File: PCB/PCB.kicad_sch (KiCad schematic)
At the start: 27 parts, among them J1 USB_C_Receptacle_USB2.0_16P, SW1 SW_Push, U1 RP2040, U2 USBLC6-2SC6, U3 NCP1117ST33T3G, Y1 Crystal_GND24

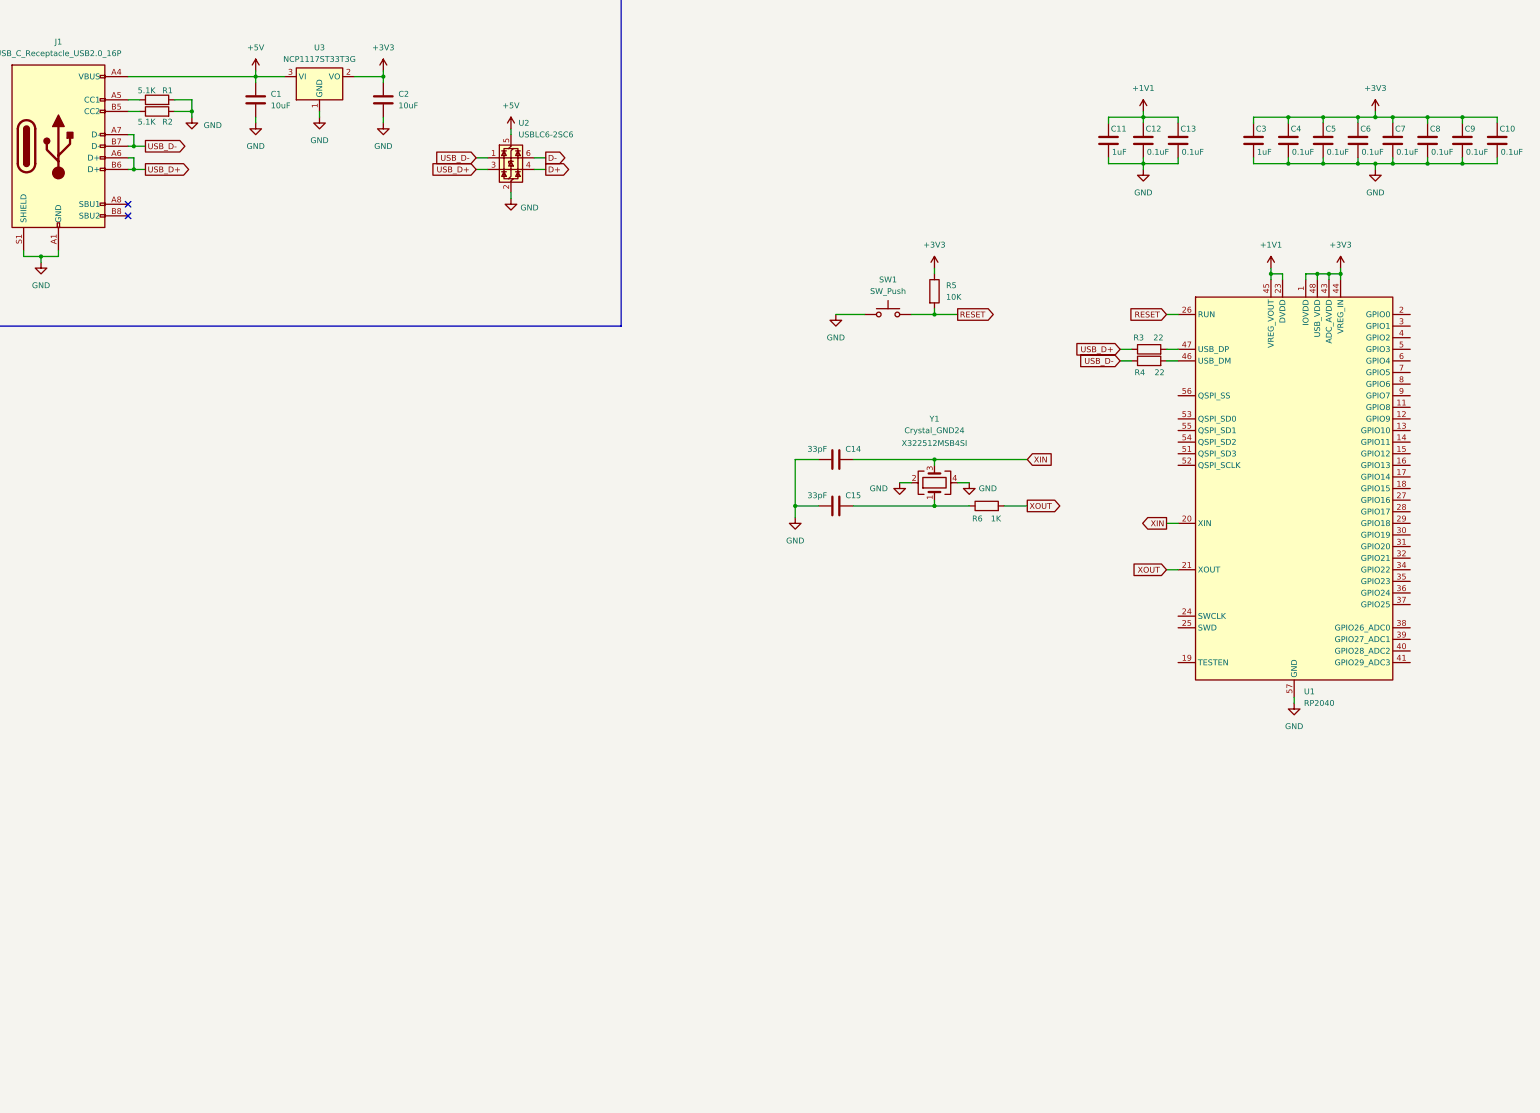
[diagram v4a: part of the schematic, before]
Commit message: added the flash
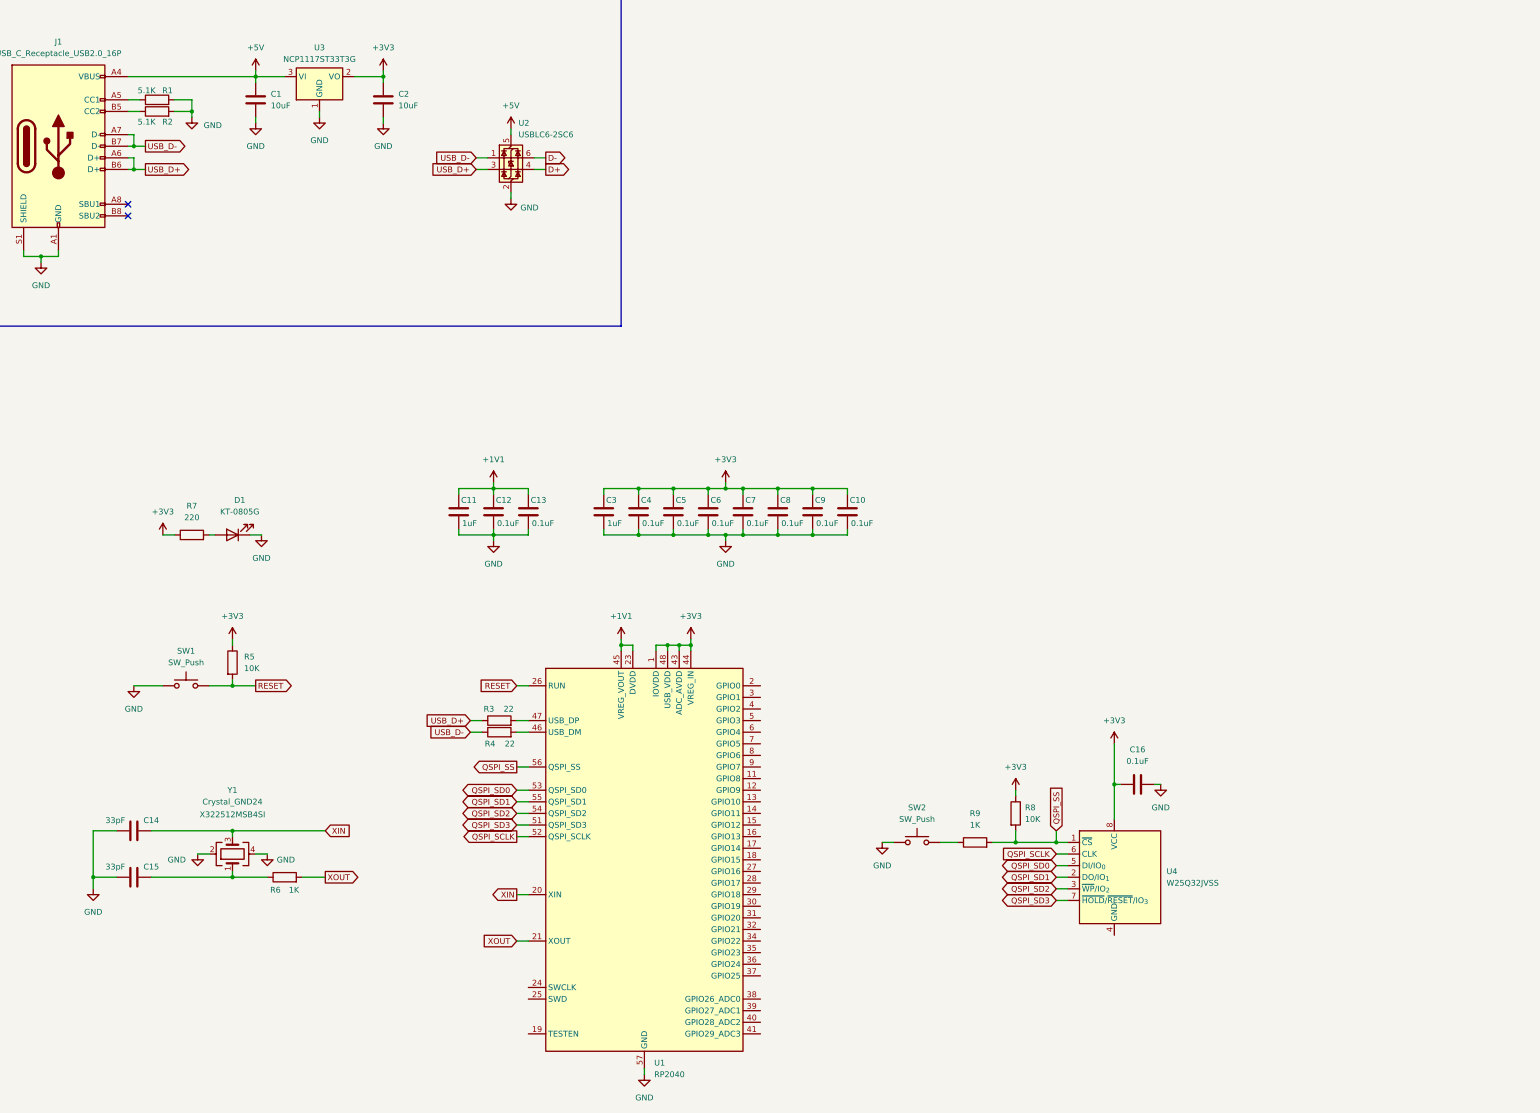
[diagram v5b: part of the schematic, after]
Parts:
- added C16: 0.1uF, symbol Device:C
- added D1: KT-0805G, symbol Device:LED
- added R7: 220, symbol Device:R
- added R8: 10K, symbol Device:R
- added R9: 1K, symbol Device:R
- added SW2: SW_Push, symbol Switch:SW_Push
- added U4: W25Q32JVSS, Package_SO:SOIC-8_5.3x5.3mm_P1.27mm, symbol Memory_Flash:W25Q32JVSS
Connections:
- net +3V3: now also C16.1, R7.1, R8.1, U4.8 (VCC)
- net GND: now also C16.2, D1.1 (K), SW2.1
- net QSPI_SD3: now reaches U1.51 (QSPI_SD3)
- net QSPI_SD3: now also U4.7 (~{HOLD}/~{RESET}/IO_{3})
- net QSPI_SCLK: now reaches U1.52 (QSPI_SCLK)
- net QSPI_SCLK: now also U4.6 (CLK)
- net QSPI_SD0: now reaches U1.53 (QSPI_SD0)
- net QSPI_SD0: now also U4.5 (DI/IO_{0})
- net QSPI_SD2: now reaches U1.54 (QSPI_SD2)
- net QSPI_SD2: now also U4.3 (~{WP}/IO_{2})
- net QSPI_SD1: now reaches U1.55 (QSPI_SD1)
- net QSPI_SD1: now also U4.2 (DO/IO_{1})
- net QSPI_SS: now reaches U1.56 (QSPI_SS)
- net QSPI_SS: now also R8.2, R9.2, U4.1 (~{CS})
- new net: R9.1, SW2.2
- new net: D1.2 (A), R7.2
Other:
- moved on the sheet: C10, C11, C12, C13, C14, C15, C3, C4, C5, C6, C7, C8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

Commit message: added the FPC connector in
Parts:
- added FPC1: AFC07-S24FCA-00, easyeda2kicad:FPC-SMD_AFC07-S24FCA-00, symbol easyeda2kicad:AFC07-S24FCA-00
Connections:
- net GND: now also U4.4 (GND)
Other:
- note added: "https://www.waveshare.com/w/upload/8/87/E-Paper-Driver-HAT-Schematic.pdf"
- moved on the sheet: C10, C11, C12, C13, C14, C15, C16, C3, C4, C5, C6, C7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

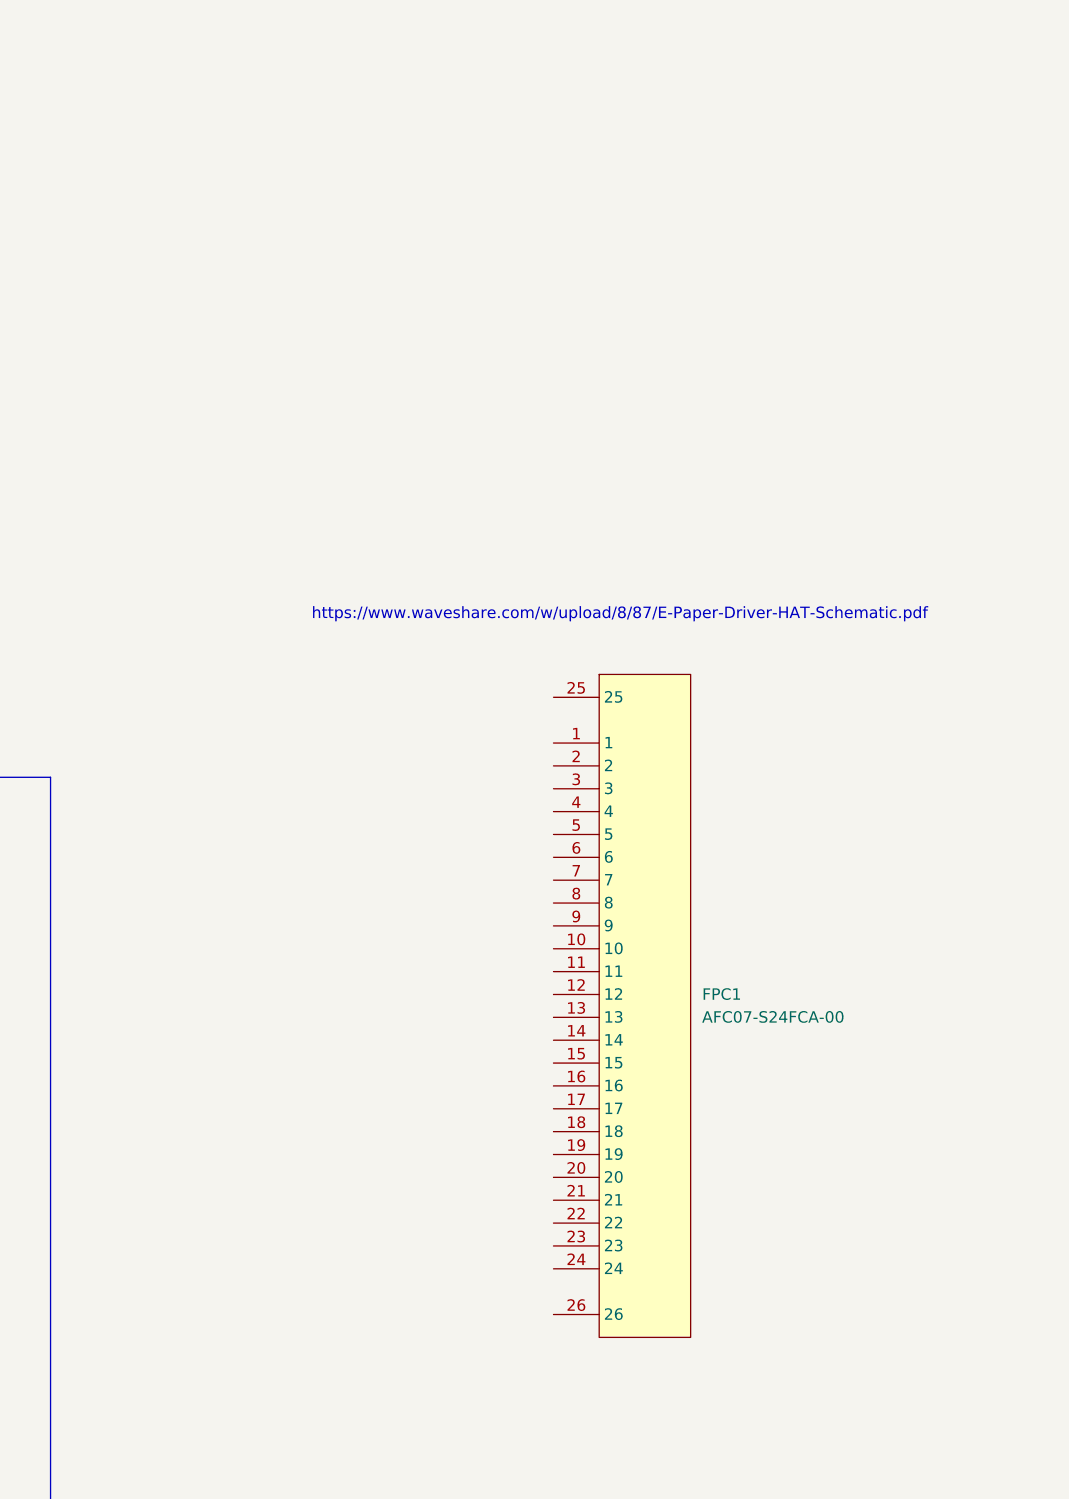
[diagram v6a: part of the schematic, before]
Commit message: changing the FPC symbol and starting to wire it
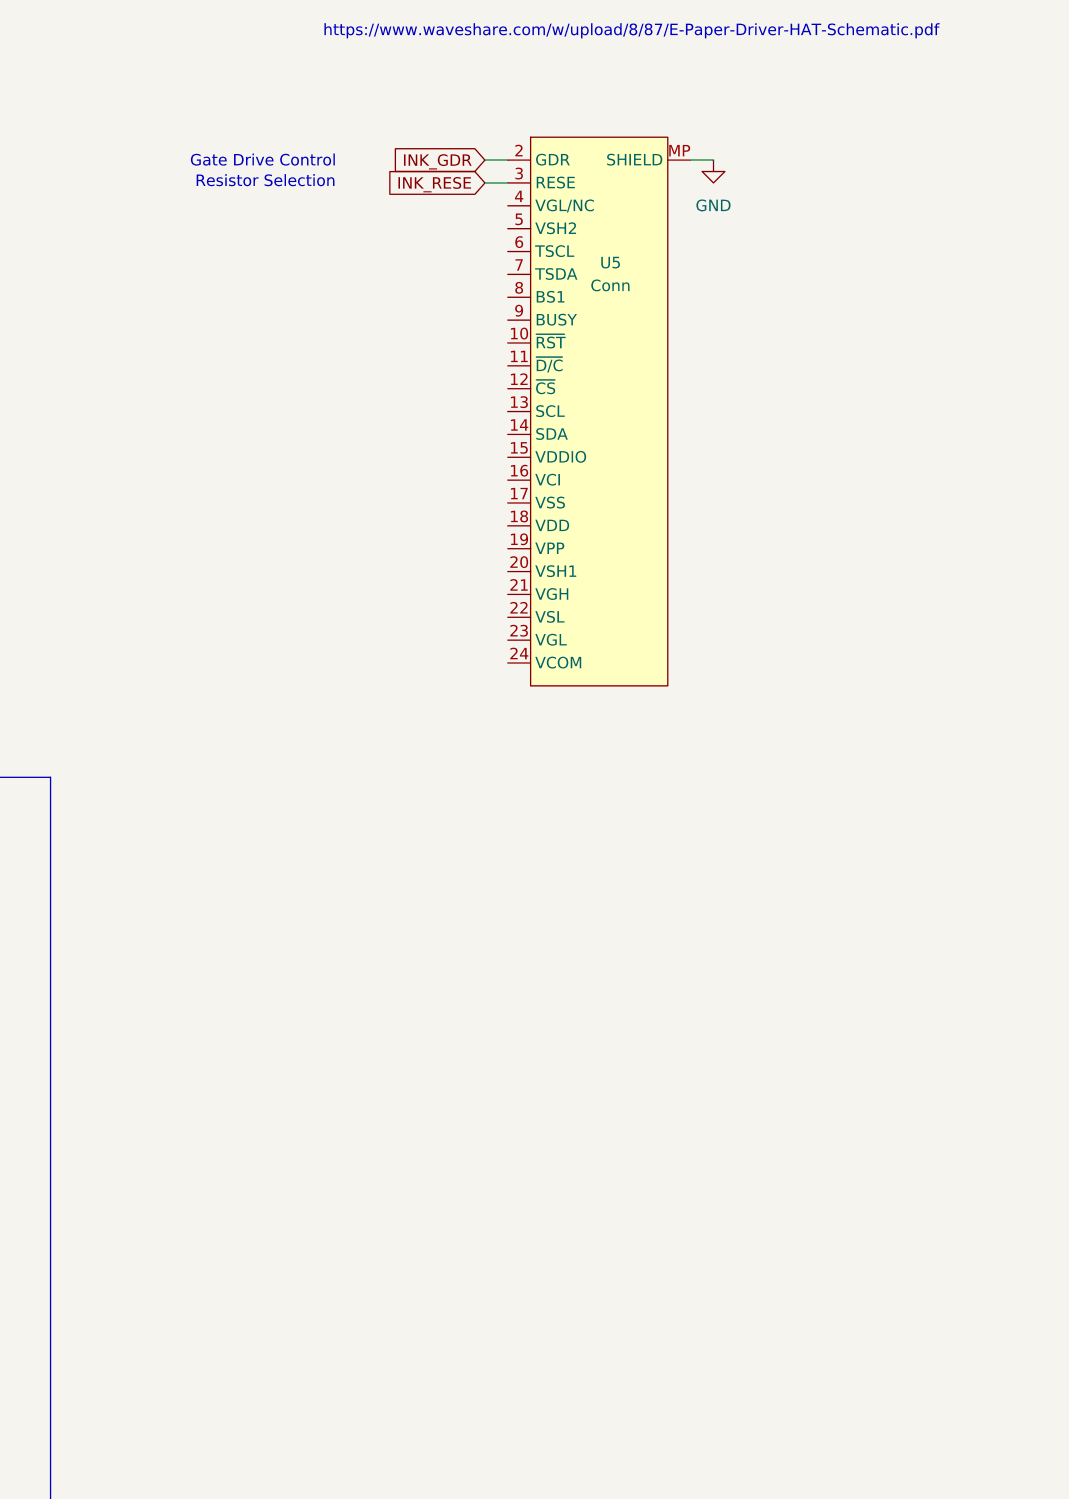
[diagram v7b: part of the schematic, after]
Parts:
- removed FPC1: AFC07-S24FCA-00, easyeda2kicad:FPC-SMD_AFC07-S24FCA-00, symbol easyeda2kicad:AFC07-S24FCA-00
- added U5: Conn, inkbadge:LCSC_1x24-1MP_P0.5mm_Horizontal, symbol inkbadge:EINK-2.9inch
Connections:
- net GND: now also U5.MP (SHIELD)
- new net INK_GDR: U5.2 (GDR)
- new net INK_RESE: U5.3 (RESE)
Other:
- note added: "Gate Drive Control"
- note added: "Resistor Selection"
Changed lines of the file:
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@@
 	(text "https://www.waveshare.com/w/upload/8/87/E-Paper-Driver-HAT-Schematic.pdf"
 		(exclude_from_sim no)
-		(at 356.616 77.216 0)
+		(at 357.886 12.446 0)
+		(effects
+			(font
+				(size 1.27 1.27)
+			)
+		)
+	)
+	(text "Resistor Selection"
+		(exclude_from_sim no)
+		(at 317.246 29.21 0)
+		(effects
+			(font
+				(size 1.27 1.27)
+			)
+		)
+	)
+	(text "Gate Drive Control"
+		(exclude_from_sim no)
+		(at 316.992 26.924 0)
 		(effects
 			(font
@@
 	(wire
 		(pts
+			(xy 341.63 26.67) (xy 344.17 26.67)
+		)
+		(stroke
+			(width 0)
+			(type default)
+		)
+	)
+	(wire
+		(pts
 			(xy 124.46 181.61) (xy 127 181.61)
 		)
@@
 	(wire
 		(pts
+			(xy 341.63 29.21) (xy 344.17 29.21)
+		)
+		(stroke
+			(width 0)
+			(type default)
+		)
+	)
+	(wire
+		(pts
 			(xy 57.15 138.43) (xy 58.42 138.43)
 		)
@@
 	(wire
 		(pts
+			(xy 367.03 26.67) (xy 364.49 26.67)
+		)
+		(stroke
+			(width 0)
+			(type default)
+		)
+	)
+	(wire
+		(pts
 			(xy 111.76 138.43) (xy 119.38 138.43)
 		)
@@
 		)
 	)
+	(global_label "INK_RESE"
+		(shape input)
+		(at 341.63 29.21 180)
+		(fields_autoplaced yes)
+		(effects
+			(font
+				(size 1.27 1.27)
+			)
+			(justify right)
+		)
+		(property "Intersheetrefs" "${INTERSHEET_REFS}"
+			(at 329.6944 29.21 0)
+			(effects
+				(font
+					(size 1.27 1.27)
+				)
+				(justify right)
+				(hide yes)
+			)
+		)
+	)
+	(global_label "INK_GDR"
+		(shape input)
+		(at 341.63 26.67 180)
+		(fields_autoplaced yes)
+		(effects
+			(font
+				(size 1.27 1.27)
+			)
+			(justify right)
+		)
+		(property "Intersheetrefs" "${INTERSHEET_REFS}"
+			(at 330.6619 26.67 0)
+			(effects
+				(font
+					(size 1.27 1.27)
+				)
+				(justify right)
+				(hide yes)
+			)
+		)
+	)
 	(global_label "QSPI_SD2"
 		(shape bidirectional)
@@
 	)
 	(symbol
+		(lib_id "inkbadge:EINK-2.9inch")
+		(at 355.6 57.15 0)
+		(unit 1)
+		(exclude_from_sim no)
+		(in_bom yes)
+		(on_board yes)
+		(dnp no)
+		(fields_autoplaced yes)
+		(property "Reference" "U5"
+			(at 355.6 38.1 0)
+			(effects
+				(font
+					(size 1.27 1.27)
+				)
+			)
+		)
+		(property "Value" "Conn"
+			(at 355.6 40.64 0)
+			(effects
+				(font
+					(size 1.27 1.27)
+				)
+			)
+		)
+		(property "Footprint" "inkbadge:LCSC_1x24-1MP_P0.5mm_Horizontal"
+			(at 355.6 57.15 0)
+			(effects
+				(font
+					(size 1.27 1.27)
+				)
+				(hide yes)
+			)
+		)
+		(property "Datasheet" ""
+			(at 355.6 57.15 0)
+			(effects
+				(font
+					(size 1.27 1.27)
+				)
+				(hide yes)
+			)
+		)
+		(property "Description" ""
+			(at 355.6 57.15 0)
+			(effects
+				(font
+					(size 1.27 1.27)
+				)
+				(hide yes)
+			)
+		)
+		(property "LCSC Part #" "C262567"
+			(at 355.6 57.15 0)
+			(effects
+				(font
+					(size 1.27 1.27)
+				)
+				(hide yes)
+			)
+		)
+		(pin "18"
+		)
+		(pin "12"
+		)
+		(pin "23"
+		)
+		(pin "19"
+		)
+		(pin "15"
+		)
+		(pin "1"
+		)
+		(pin "17"
+		)
+		(pin "10"
+		)
+		(pin "2"
+		)
+		(pin "9"
+		)
+		(pin "13"
+		)
+		(pin "20"
+		)
+		(pin "6"
+		)
+		(pin "16"
+		)
+		(pin "22"
+		)
+		(pin "11"
+		)
+		(pin "14"
+		)
+		(pin "4"
+		)
+		(pin "21"
+		)
+		(pin "24"
+		)
+		(pin "8"
+		)
+		(pin "7"
+		)
+		(pin "5"
+		)
+		(pin "3"
+		)
+		(pin "MP"
+		)
+		(instances
+			(project "PCB"
+				(path "/f82e74e4-6971-48c6-8666-d0a9e9f61139"
+					(reference "U5")
+					(unit 1)
+				)
+			)
+		)
+	)
+	(symbol
 		(lib_id "power:+3V3")
 		(at 162.56 161.29 0)
@@
 	)
 	(symbol
+		(lib_id "power:GND")
+		(at 367.03 26.67 0)
+		(unit 1)
+		(exclude_from_sim no)
+		(in_bom yes)
+		(on_board yes)
+		(dnp no)
+		(fields_autoplaced yes)
+		(property "Reference" "#PWR029"
+			(at 367.03 33.02 0)
+			(effects
+				(font
+					(size 1.27 1.27)
+				)
+				(hide yes)
+			)
+		)
+		(property "Value" "GND"
+			(at 367.03 31.75 0)
+			(effects
+				(font
+					(size 1.27 1.27)
+				)
+			)
+		)
+		(property "Footprint" ""
+			(at 367.03 26.67 0)
+			(effects
+				(font
+					(size 1.27 1.27)
+				)
+				(hide yes)
+			)
+		)
+		(property "Datasheet" ""
+			(at 367.03 26.67 0)
+			(effects
+				(font
+					(size 1.27 1.27)
+				)
+				(hide yes)
+			)
+		)
+		(property "Description" "Power symbol creates a global label with name \"GND\" , ground"
+			(at 367.03 26.67 0)
+			(effects
+				(font
+					(size 1.27 1.27)
+				)
+				(hide yes)
+			)
+		)
+		(pin "1"
+		)
+		(instances
+			(project ""
+				(path "/f82e74e4-6971-48c6-8666-d0a9e9f61139"
+					(reference "#PWR029")
+					(unit 1)
+				)
+			)
+		)
+	)
+	(symbol
 		(lib_id "power:+3V3")
 		(at 233.68 194.31 0)
@@
 					(unit 1)
 				)
-			)
-		)
-	)
-	(symbol
-		(lib_id "easyeda2kicad:AFC07-S24FCA-00")
-		(at 356.87 120.65 0)
-		(unit 1)
-		(exclude_from_sim no)
-		(in_bom yes)
-		(on_board yes)
-		(dnp no)
-		(fields_autoplaced yes)
-		(property "Reference" "FPC1"
-			(at 365.76 119.3799 0)
-			(effects
-				(font
-					(size 1.27 1.27)
-				)
-				(justify left)
-			)
-		)
-		(property "Value" "AFC07-S24FCA-00"
-			(at 365.76 121.9199 0)
-			(effects
-				(font
-					(size 1.27 1.27)
-				)
-				(justify left)
-			)
-		)
-		(property "Footprint" "easyeda2kicad:FPC-SMD_AFC07-S24FCA-00"
-			(at 356.87 162.56 0)
-			(effects
-				(font
-					(size 1.27 1.27)
-				)
-				(hide yes)
-			)
-		)
-		(property "Datasheet" "https://lcsc.com/product-detail/Others_JUSHUO-AFC07-S24FCA-00_C262567.html"
-			(at 356.87 165.1 0)
-			(effects
-				(font
-					(size 1.27 1.27)
-				)
-				(hide yes)
-			)
-		)
-		(property "Description" ""
-			(at 356.87 120.65 0)
-			(effects
-				(font
-					(size 1.27 1.27)
-				)
-				(hide yes)
-			)
-		)
-		(property "LCSC Part" "C262567"
-			(at 356.87 167.64 0)
-			(effects
-				(font
-					(size 1.27 1.27)
-				)
-				(hide yes)
-			)
-		)
-		(pin "17"
-		)
-		(pin "16"
-		)
-		(pin "19"
-		)
-		(pin "22"
-		)
-		(pin "25"
-		)
-		(pin "1"
-		)
-		(pin "2"
-		)
-		(pin "4"
-		)
-		(pin "3"
-		)
-		(pin "24"
-		)
-		(pin "13"
-		)
-		(pin "8"
-		)
-		(pin "10"
-		)
-		(pin "15"
-		)
-		(pin "12"
-		)
-		(pin "5"
-		)
-		(pin "9"
-		)
-		(pin "18"
-		)
-		(pin "11"
-		)
-		(pin "7"
-		)
-		(pin "14"
-		)
-		(pin "26"
-		)
-		(pin "21"
-		)
-		(pin "20"
-		)
-		(pin "6"
-		)
-		(pin "23"
-		)
-		(instances
-			(project ""
-				(path "/f82e74e4-6971-48c6-8666-d0a9e9f61139"
-					(reference "FPC1")
-					(unit 1)
-				)
